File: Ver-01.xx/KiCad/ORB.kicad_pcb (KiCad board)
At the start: 2 copper layers, 104 x 72 mm, 140 parts, among them IC1 LM3940-3.3, IC2 LM340-5.0, IC3 LM340-5.0, IC4 TB6612FNG, IC5 TB6612FNG, J1 LOETJUMPER, J2 USB_C_Receptacle_USB2.0, J3 Conn_02x03_Odd_Even, K10 NXT-Socket, K11 NXT-Socket, K12 Wannenstecker, K13 Wannenstecker, K14 NXT-Socket, K15 Stiftleiste_1x06, K16 NXT-Socket, K17 Wannenstecker, K18 Wannenstecker, K19 NXT-Socket, K2 Anschlussklemme, K20 NXT-Socket, K21 Wannenstecker, K24 Stiftleiste_2x02, K25 Stiftleiste_1x04, K26 Stiftleiste_1x02_G_2,54, K4 Wannenstecker, K6 NXT-Socket, K7 NXT-Socket, K8 Wannenstecker, K9 Wannenstecker, U1 RN4678, X1 STM32F405VGT, Y1 Crystal

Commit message: New Logo
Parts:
- added R17: 1M, Resistor_SMD:R_0603_1608Metric, F.Cu at (115.3, 82.0)
- moved REF** 1.22 mm to (149.7, 80.7)
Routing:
- net GND: vias 42 -> 44

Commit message: Kleinere Optimierungen
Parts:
- R5: value 10k -> 10K
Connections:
- X1 pad 45: M1-IN1 -> M1-IN2
- X1 pad 46: M1-IN2 -> M1-IN1
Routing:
- net M1-IN1: track 14.2 -> 13.1 mm, vias 2 -> 0
- net ENCB-2-IO: track 63.8 -> 62.9 mm
- net ENCA-2-IO: track 65.6 -> 65.0 mm
- net SERVO_PWM_EXT_2: track 47.4 -> 46.8 mm

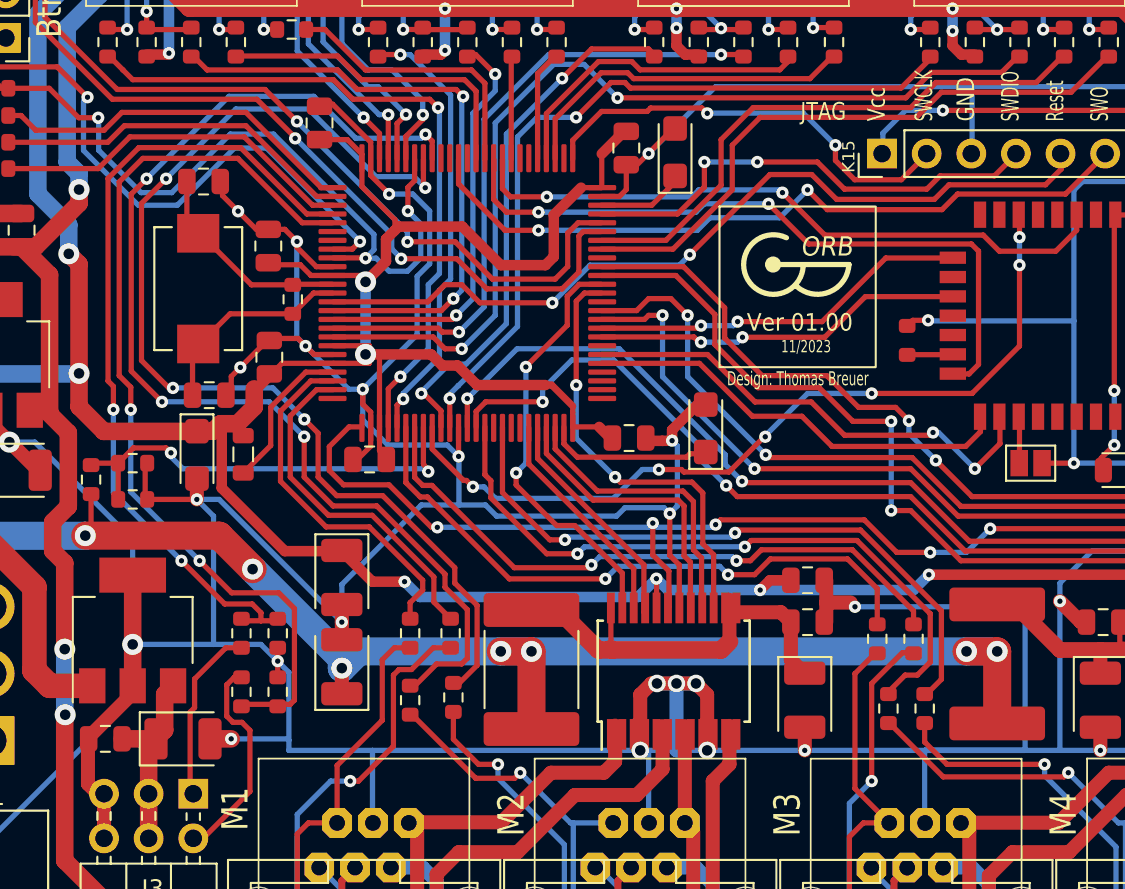
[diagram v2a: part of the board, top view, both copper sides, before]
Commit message: R (Crystal) raus, C (Reset) hinzu
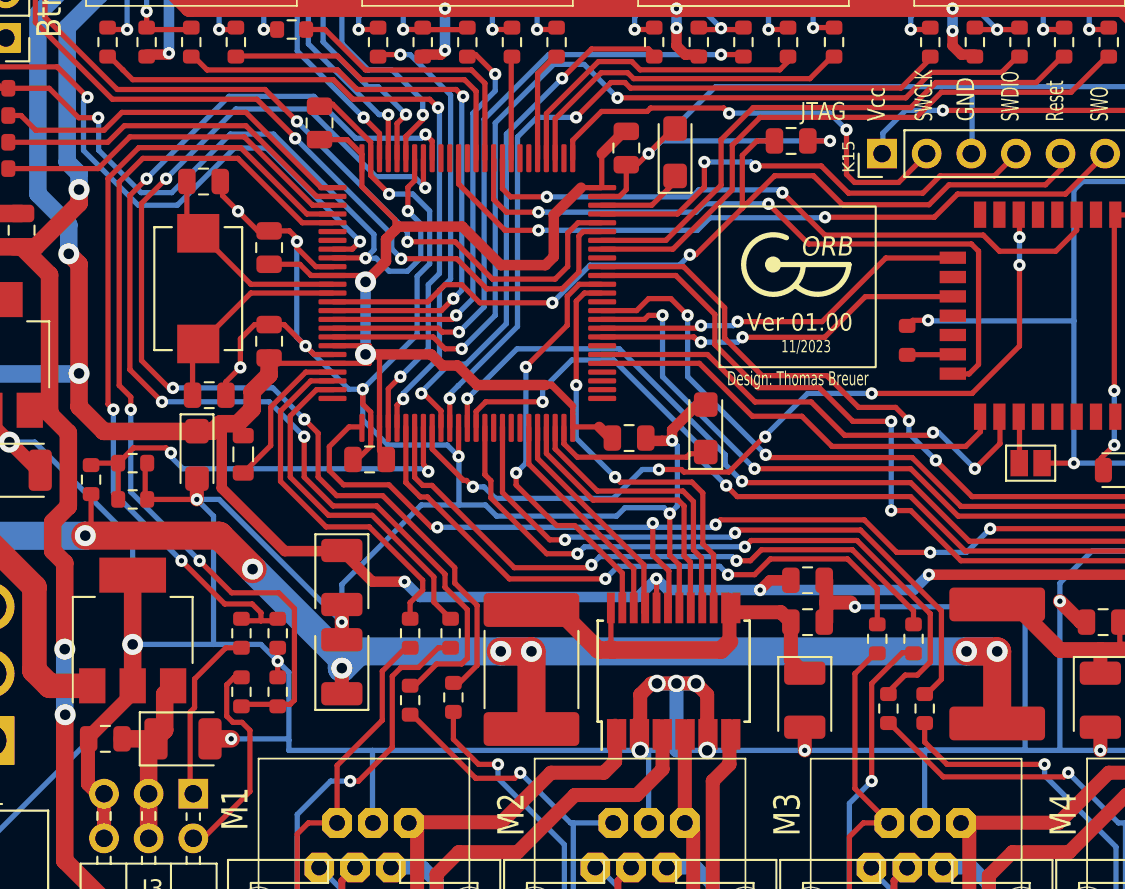
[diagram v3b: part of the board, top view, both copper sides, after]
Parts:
- removed R17: 1M, Resistor_SMD:R_0603_1608Metric
- added C31: 100nF, Capacitor_SMD:C_0805_2012Metric, F.Cu at (143.7, 72.9)
- moved C15 0.91 mm to (114.0, 84.3)
- moved C14 0.10 mm to (114.0, 79.0)
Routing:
- net GND: track 874.9 -> 888.6 mm, vias 44 -> 45
- net /Controller, Bluetooth/RESET: track 47.5 -> 52.8 mm
- net /Controller, Bluetooth/JTAG_TCLK_SWCLK: track 24.9 -> 26.0 mm
- net /Controller, Bluetooth/JTAG_TDO_SWO: track 42.1 -> 41.2 mm
- net +3V3: track 359.9 -> 360.6 mm

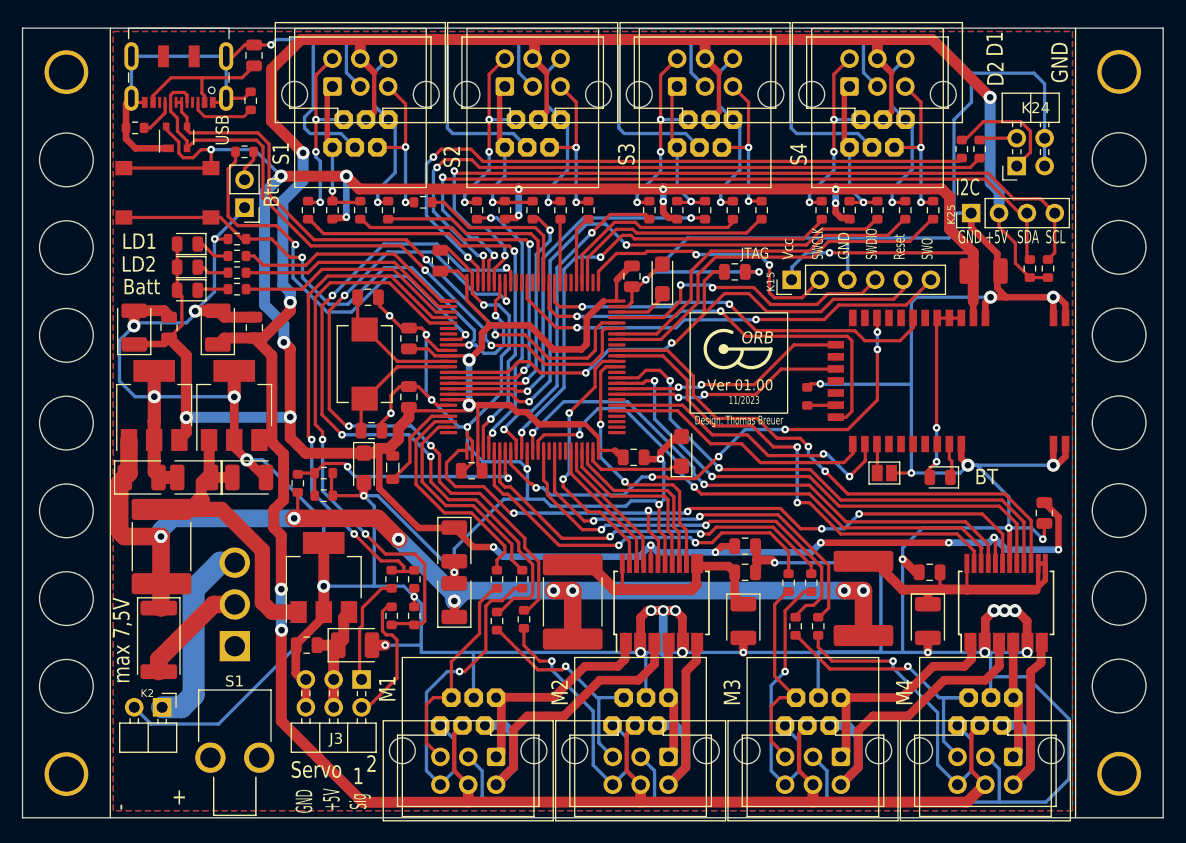
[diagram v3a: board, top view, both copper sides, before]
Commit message: Review
- New Crystal
- GND plane on front side
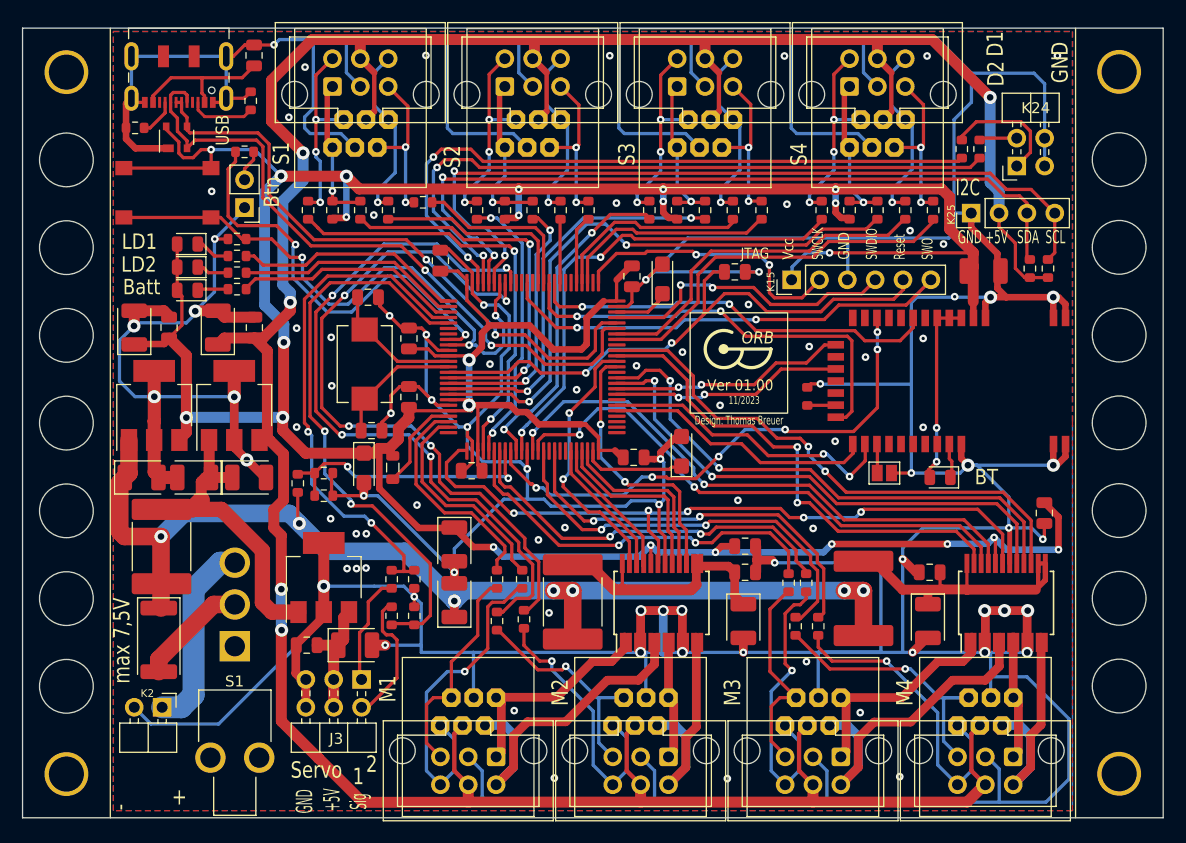
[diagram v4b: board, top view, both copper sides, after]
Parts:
- moved R39 0.46 mm to (150.2, 101.3)
- renumbered REF** to Logo**
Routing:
- net GND: track 888.6 -> 870.6 mm, vias 45 -> 92
- net +5V_Sensor: track 289.7 -> 288.8 mm
- net ENCB-2-IO: track 62.9 -> 63.8 mm
- net +3V3: track 360.6 -> 360.0 mm
- net /Motor-Ports/MOTORP-1: track 21.0 -> 20.4 mm
- net ENCA-2-IO: track 65.1 -> 65.7 mm
- net /Controller, Bluetooth/BT_STATUS: track 47.3 -> 47.9 mm
- net I2C_SDA: track 71.2 -> 71.7 mm
- net +Vin: track 103.9 -> 104.0 mm, vias 8 -> 7

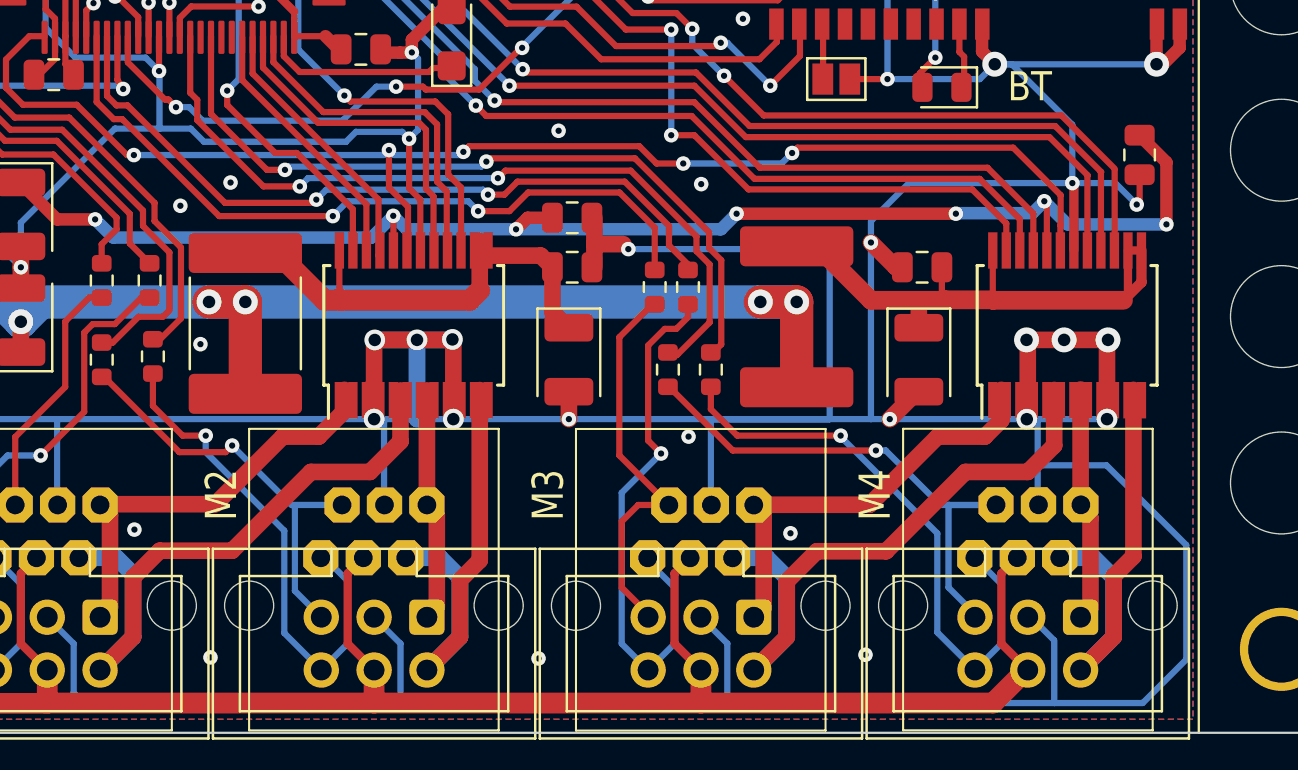
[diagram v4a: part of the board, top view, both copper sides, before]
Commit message: Abstand MotorX-Y kleiner
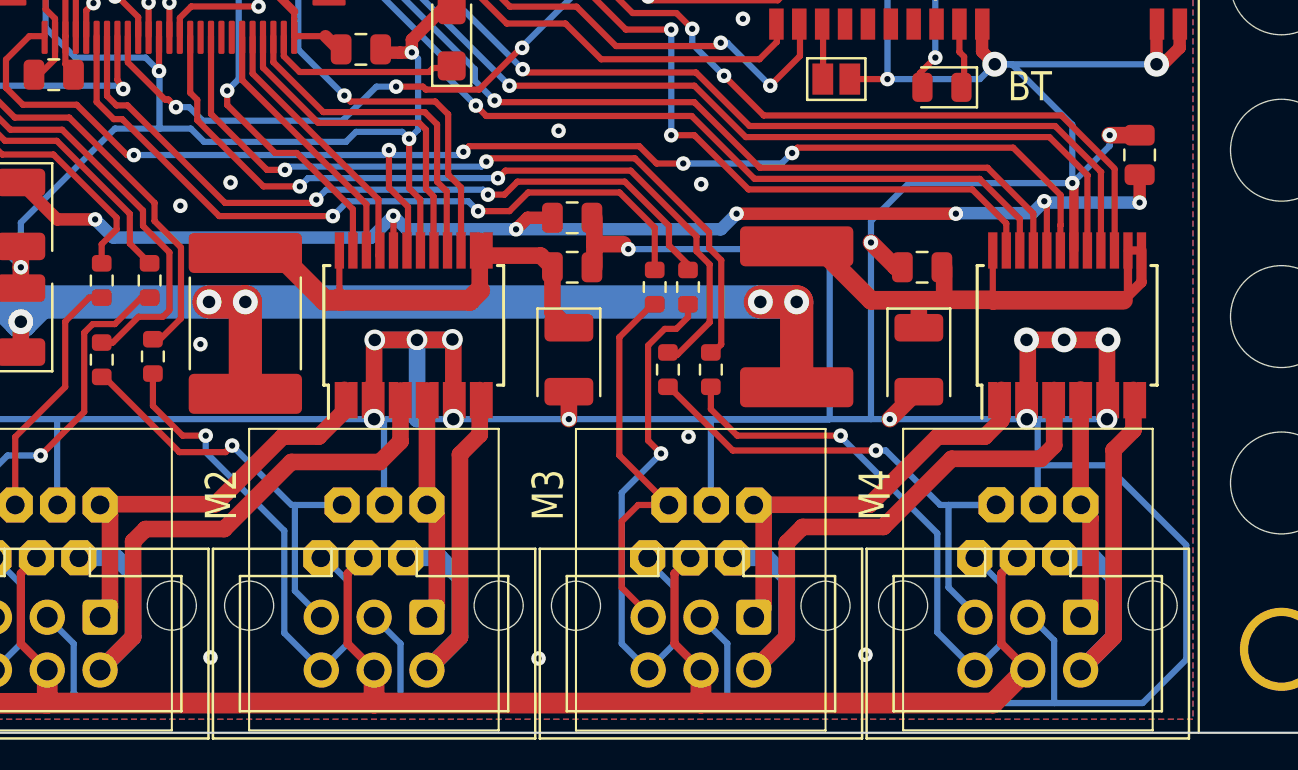
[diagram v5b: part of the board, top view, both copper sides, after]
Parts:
- turned C30 to -90 degrees
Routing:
- net +3V3: track 360.0 -> 354.8 mm
- net /Motor-Ports/MOTORM-3: track 31.3 -> 32.4 mm
- net /Motor-Ports/MOTORM-1: track 31.3 -> 32.3 mm
- net GND: track 870.6 -> 870.1 mm, vias 92 -> 90

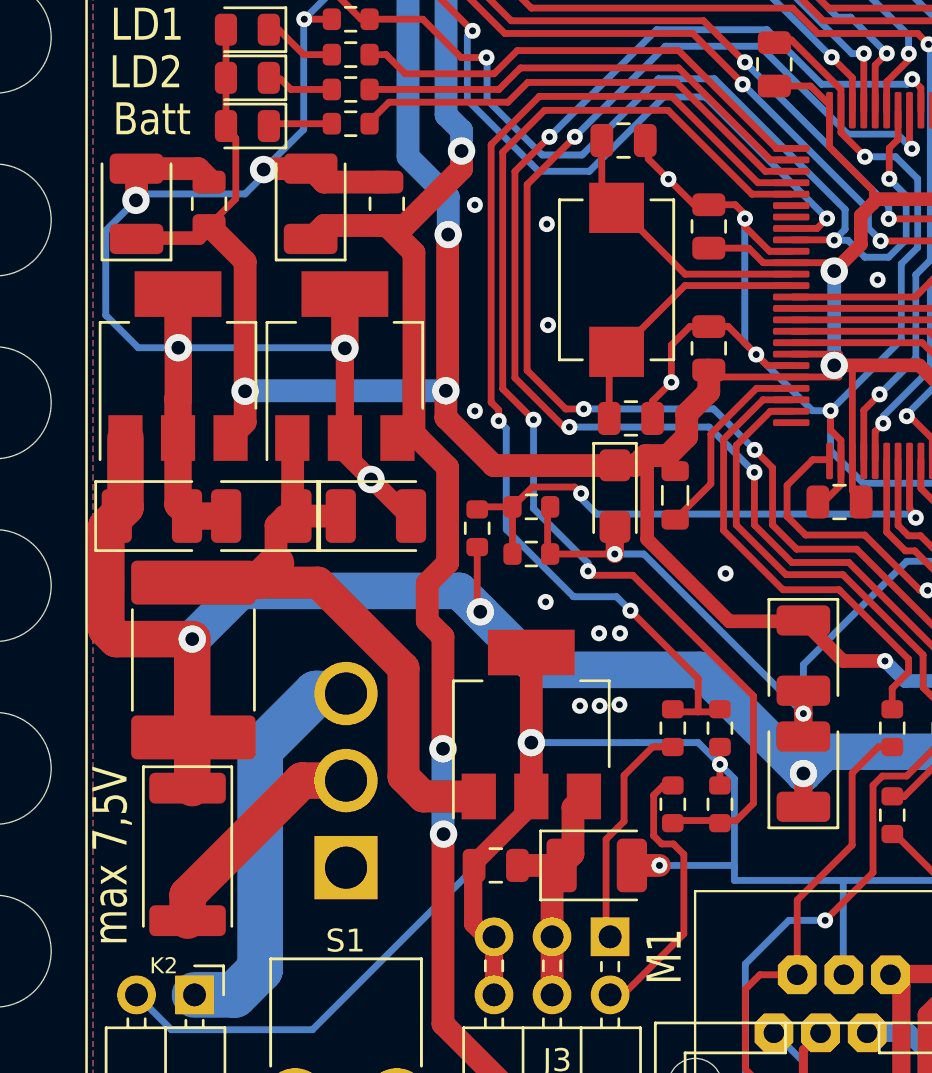
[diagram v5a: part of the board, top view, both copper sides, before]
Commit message: After production test
Footprint D1 and Y1 changed.
LED shunt R=330
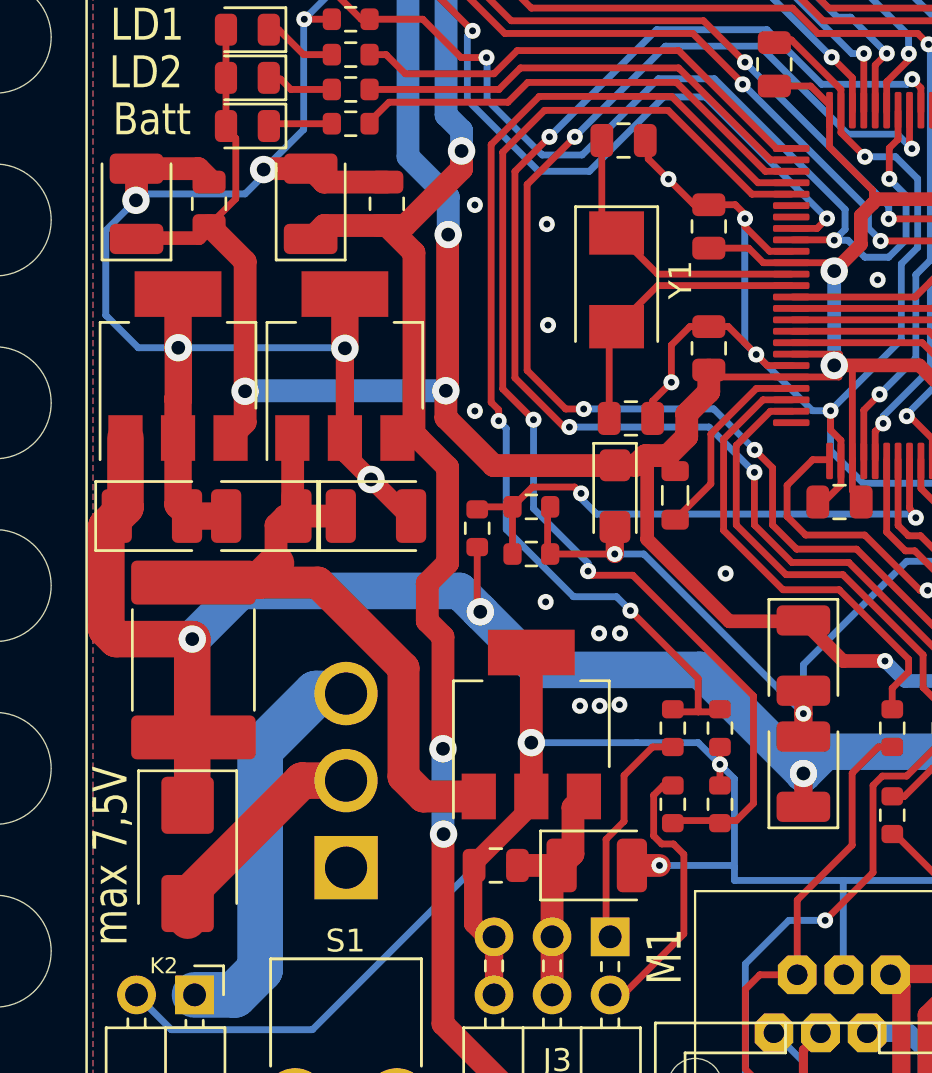
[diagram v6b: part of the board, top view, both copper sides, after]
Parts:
- D1: footprint Diode_SMD:D_2512_6332Metric -> Diode_SMD:D_SMB
- R2, R4, R6: value 75 -> 330
- Y1: footprint ORB:XTAL_ECS-80-20-20A-TR -> Crystal:Crystal_SMD_Abracon_ABM3-2Pin_5.0x3.2mm
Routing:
- net Net-(X1-PH1/OSC_OUT): track 11.8 -> 12.5 mm
- net Net-(X1-PH0/OSC_IN): track 12.0 -> 12.7 mm
